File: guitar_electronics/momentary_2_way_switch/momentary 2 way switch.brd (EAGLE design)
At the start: 15 x 17 mm, 8 parts

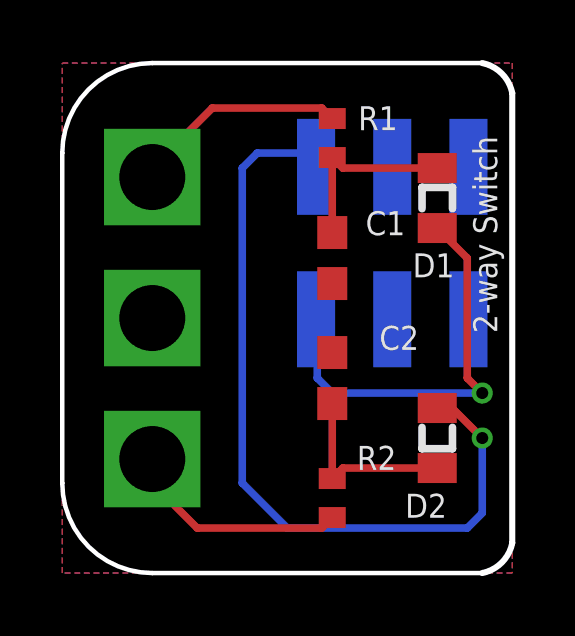
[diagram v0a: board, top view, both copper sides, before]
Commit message: updates for 2 way switch
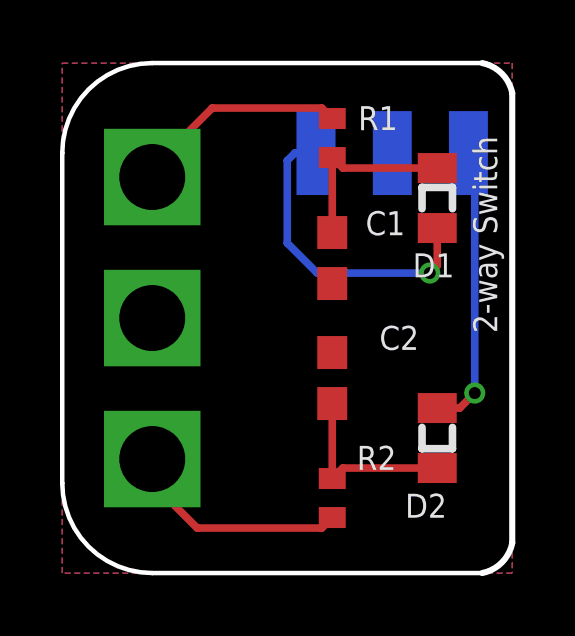
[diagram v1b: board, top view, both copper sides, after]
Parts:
- H1: value 6PIN-SMD-2.54MM_2 -> 3PIN-SMD-2.54MM; device CYCFI_Con:6P-SMD-2.54_2 -> CYCFI_Con:3P-SMD-2.54MM
- moved H1 3.00 mm to (11.0, 14.0), turned to 180 degrees
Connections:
- net GND: now also H1.P$2; no longer H1.P2, H1.P5
- net SW1: now also H1.P$3; no longer H1.P1
- net SW2: now also H1.P$1; no longer H1.P6
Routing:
- net SW1: track 26.6 -> 9.54 mm
- net SW2: track 13.8 -> 10.6 mm
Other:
- board text added: "DOWN"
- board text added: "UP"
- board text removed: "NC"
- board text removed: "OUT"
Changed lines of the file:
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@@
 <setting verticaltext="up"/>
 </settings>
-<grid distance="0.5" unitdist="mm" unit="mm" style="lines" multiple="1" display="yes" altdistance="0.25" altunitdist="mm" altunit="mm"/>
+<grid distance="0.25" unitdist="mm" unit="mm" style="lines" multiple="1" display="yes" altdistance="0.25" altunitdist="mm" altunit="mm"/>
 <layers>
 <layer number="1" name="Top" color="4" fill="1" visible="yes" active="yes"/>
@@
 <wire x1="14" y1="17" x2="15" y2="16" width="0.2032" layer="20" curve="-67.380135"/>
 <text x="14.5" y="8" size="0.8" layer="25" font="vector" ratio="14" rot="R90">2-way Switch</text>
-<text x="9.25" y="15.5" size="0.6096" layer="26" font="vector" ratio="14" rot="MR0">OUT</text>
-<text x="11.75" y="15.5" size="0.6096" layer="26" font="vector" ratio="14" rot="MR0">GND</text>
-<text x="14" y="15.5" size="0.6096" layer="26" font="vector" ratio="14" rot="MR0">NC</text>
+<text x="9.5" y="15.75" size="0.6096" layer="26" font="vector" ratio="14" rot="MR0">DOWN</text>
+<text x="11.75" y="15.75" size="0.6096" layer="26" font="vector" ratio="14" rot="MR0">GND</text>
+<text x="14" y="15.75" size="0.6096" layer="26" font="vector" ratio="14" rot="MR0">UP</text>
 <text x="4.5" y="0.5" size="0.8128" layer="26" font="vector" rot="MR0">v2.5</text>
 </plain>
@@
 </element>
 <element name="S1" library="switch" package="SPDT" value="SPDT" x="3" y="8.5" smashed="yes" rot="R270"/>
-<element name="H1" library="CYCFI_Con" package="6P-SMD-2.54_2" value="6PIN-SMD-2.54MM_2" x="11" y="11" smashed="yes" rot="MR270"/>
+<element name="H1" library="CYCFI_Con" package="3P-SMD-2.54MM" value="3PIN-SMD-2.54MM" x="11" y="14" rot="MR180"/>
 </elements>
 <signals>
@@
 <contactref element="C2" pad="2"/>
 <contactref element="S1" pad="2"/>
-<contactref element="H1" pad="P5"/>
-<contactref element="H1" pad="P2"/>
 <polygon width="0.2032" layer="16">
 <vertex x="0" y="0"/>
@@
 <vertex x="15" y="0"/>
 </polygon>
+<contactref element="H1" pad="P$2"/>
 </signal>
 <signal name="N$1">
@@
 <signal name="SW2">
 <contactref element="D1" pad="1"/>
-<contactref element="H1" pad="P6"/>
-<wire x1="12.5" y1="11.5" x2="13.5" y2="10.5" width="0.254" layer="1"/>
-<wire x1="13.5" y1="10.5" x2="13.5" y2="6.5" width="0.254" layer="1"/>
-<wire x1="13.5" y1="6.5" x2="14" y2="6" width="0.254" layer="1"/>
-<via x="14" y="6" extent="1-16" drill="0.4"/>
-<wire x1="14" y1="6" x2="9" y2="6" width="0.254" layer="16"/>
-<wire x1="9" y1="6" x2="8.5" y2="6.5" width="0.254" layer="16"/>
-<wire x1="8.5" y1="6.5" x2="8.5" y2="8.42" width="0.254" layer="16"/>
-<wire x1="8.5" y1="8.42" x2="8.46" y2="8.46" width="0.254" layer="16"/>
+<contactref element="H1" pad="P$1"/>
+<wire x1="12.5" y1="11.5" x2="12.5" y2="10.25" width="0.254" layer="1"/>
+<wire x1="12.5" y1="10.25" x2="12.25" y2="10" width="0.254" layer="1"/>
+<via x="12.25" y="10" extent="1-16" drill="0.4"/>
+<wire x1="12.25" y1="10" x2="8.5" y2="10" width="0.254" layer="16"/>
+<wire x1="8.5" y1="10" x2="7.5" y2="11" width="0.254" layer="16"/>
+<wire x1="7.5" y1="11" x2="7.5" y2="13.75" width="0.254" layer="16"/>
+<wire x1="7.5" y1="13.75" x2="7.75" y2="14" width="0.254" layer="16"/>
+<wire x1="7.75" y1="14" x2="8.46" y2="14" width="0.254" layer="16"/>
 </signal>
 <signal name="N$2">
@@
 <signal name="SW1">
 <contactref element="D2" pad="1"/>
-<contactref element="H1" pad="P1"/>
-<wire x1="12.5" y1="5.5" x2="13" y2="5.5" width="0.254" layer="1"/>
-<wire x1="13" y1="5.5" x2="14" y2="4.5" width="0.254" layer="1"/>
-<via x="14" y="4.5" extent="1-16" drill="0.4"/>
-<wire x1="14" y1="4.5" x2="14" y2="2" width="0.254" layer="16"/>
-<wire x1="14" y1="2" x2="13.5" y2="1.5" width="0.254" layer="16"/>
-<wire x1="13.5" y1="1.5" x2="7.5" y2="1.5" width="0.254" layer="16"/>
-<wire x1="7.5" y1="1.5" x2="6" y2="3" width="0.254" layer="16"/>
-<wire x1="6" y1="3" x2="6" y2="13.5" width="0.254" layer="16"/>
-<wire x1="6" y1="13.5" x2="6.5" y2="14" width="0.254" layer="16"/>
-<wire x1="6.5" y1="14" x2="8" y2="14" width="0.254" layer="16"/>
-<wire x1="8" y1="14" x2="8.46" y2="13.54" width="0.254" layer="16"/>
+<wire x1="12.5" y1="5.5" x2="13.25" y2="5.5" width="0.254" layer="1"/>
+<contactref element="H1" pad="P$3"/>
+<wire x1="13.25" y1="5.5" x2="13.75" y2="6" width="0.254" layer="1"/>
+<via x="13.75" y="6" extent="1-16" drill="0.4"/>
+<wire x1="13.75" y1="6" x2="13.75" y2="13.79" width="0.254" layer="16"/>
+<wire x1="13.75" y1="13.79" x2="13.54" y2="14" width="0.254" layer="16"/>
 </signal>
 <signal name="N$4">

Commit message: add schematic and bom file
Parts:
- D1, D2: value (none) -> CUS551V30,H3F
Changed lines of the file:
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@@
 <attribute name="VALUE" x="6.968" y="15.135" size="0.8" layer="27" rot="R270"/>
 </element>
-<element name="D1" library="m-pad-2.1" package="SOD-323" value="" x="12.5" y="12.5" smashed="yes" rot="R90">
+<element name="D1" library="m-pad-2.1" package="SOD-323" value="CUS551V30,H3F" x="12.5" y="12.5" smashed="yes" rot="R90">
 <attribute name="NAME" x="13.07" y="10.657" size="0.8" layer="25" font="vector" rot="R180"/>
 <attribute name="VALUE" x="14.513" y="10.73" size="1.27" layer="27" rot="R90"/>
@@
 <attribute name="VALUE" x="11.032" y="1.865" size="0.8" layer="27" rot="R90"/>
 </element>
-<element name="D2" library="m-pad-2.1" package="SOD-323" value="" x="12.5" y="4.5" smashed="yes" rot="R270">
+<element name="D2" library="m-pad-2.1" package="SOD-323" value="CUS551V30,H3F" x="12.5" y="4.5" smashed="yes" rot="R270">
 <attribute name="NAME" x="11.43" y="1.843" size="0.8" layer="25" font="vector"/>
 <attribute name="VALUE" x="10.487" y="6.27" size="1.27" layer="27" rot="R270"/>
